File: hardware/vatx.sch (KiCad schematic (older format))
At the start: 26 parts, among them J1 USB, P1 CONN_10X2, P2 CONN_01X05, P3 CONN_1, P4 CONN_1, P5 CONN_1, P6 CONN_1, P7 CONN_1, SW1 SWITCH_INV, U1 LM317T

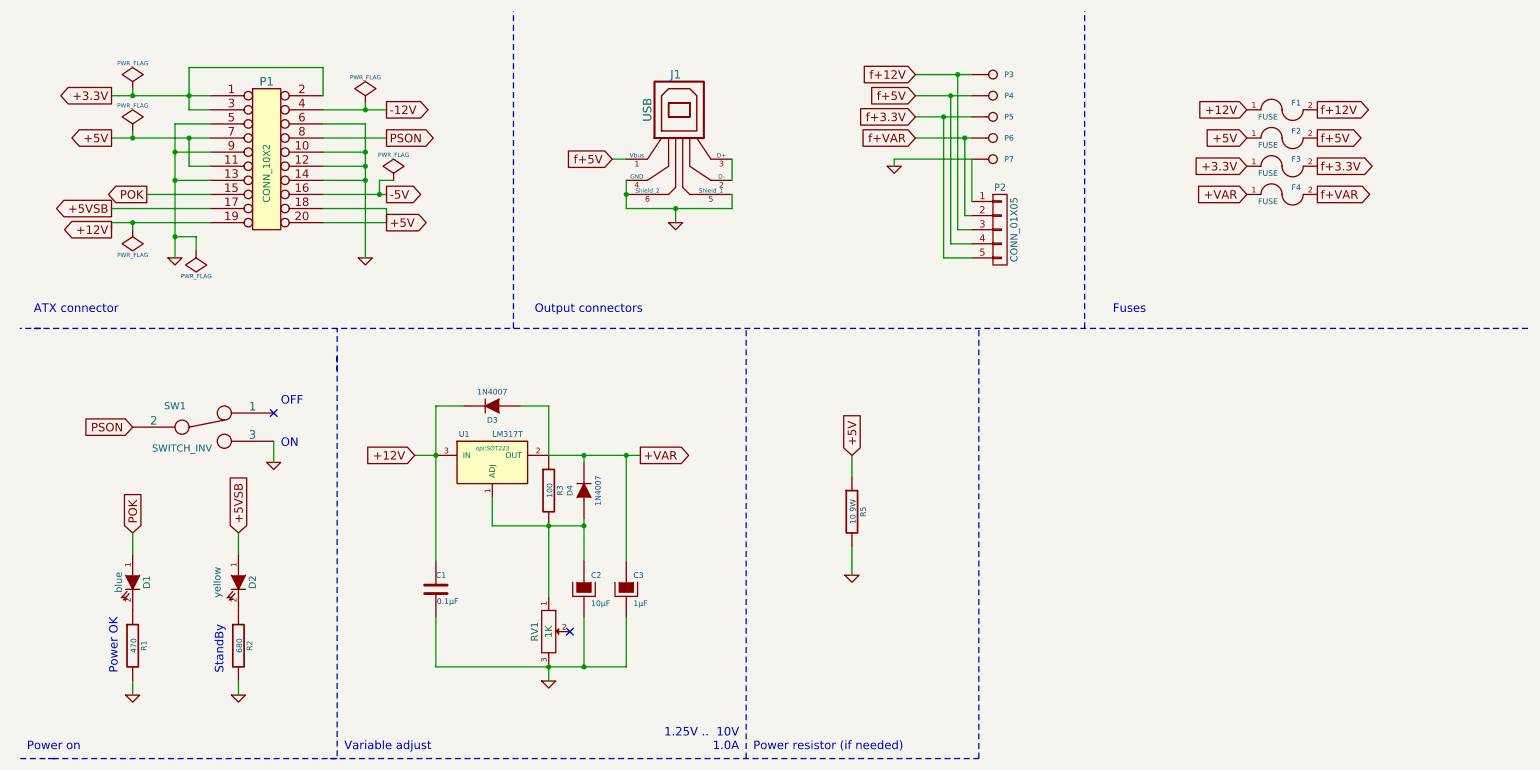
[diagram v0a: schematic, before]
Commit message: scheme for optional PSON control
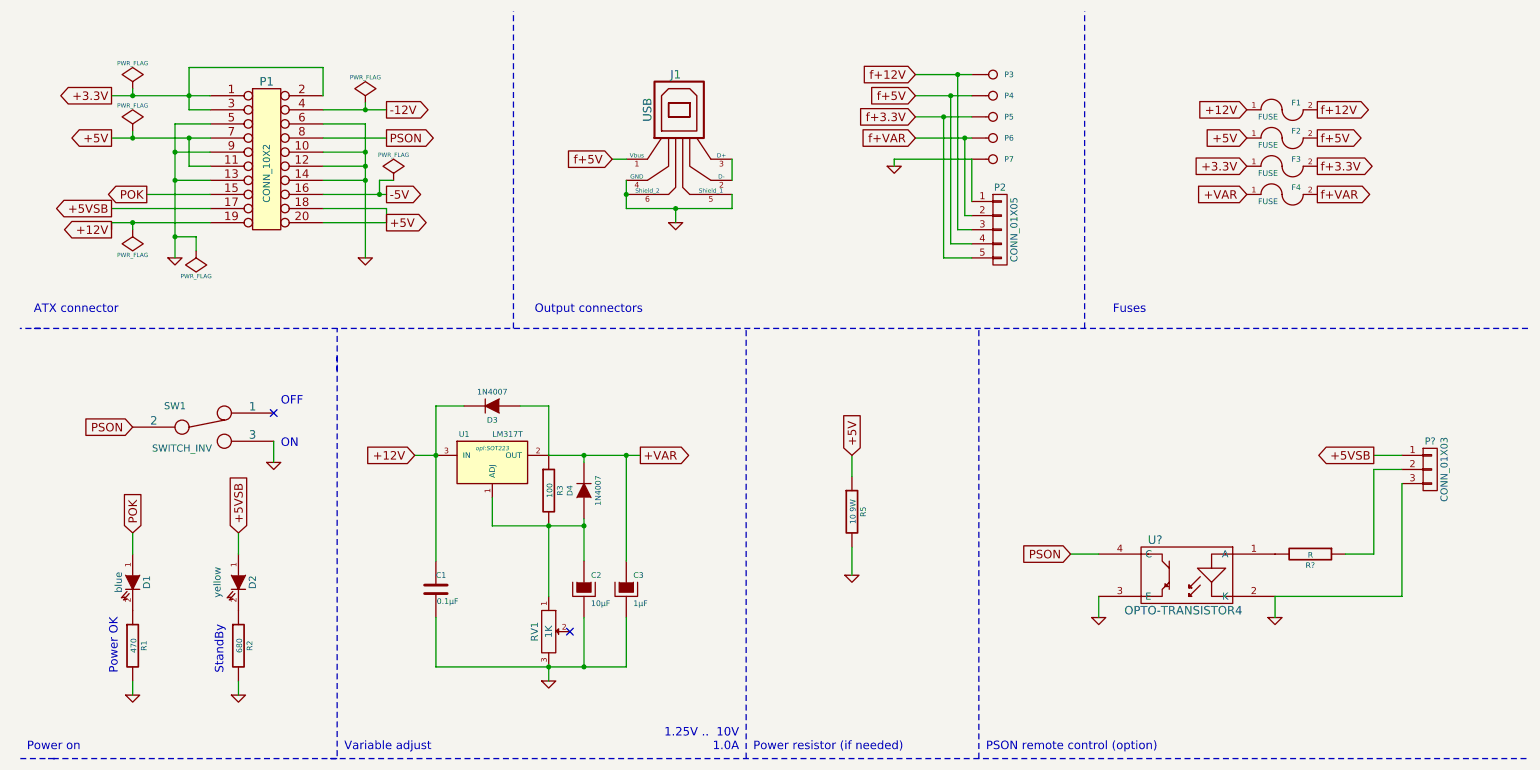
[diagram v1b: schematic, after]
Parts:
- added P?: CONN_01X03, symbol CONN_01X03
- added R?: R, symbol R
- added U?: OPTO-TRANSISTOR4, symbol OPTO-TRANSISTOR4
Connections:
- net +5VSB: now also P?.1 (P1)
- net GND: now also P?.3 (P3), U?.2 (K), U?.3 (E)
- net PSON: now also U?.4 (C)
- new net: R?.2, U?.1 (A)
- new net: P?.2 (P2), R?.1
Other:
- note added: "PSON remote control (option)"
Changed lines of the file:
@@
 Power on
 Wire Notes Line
-	2700 5800 7300 5800
+	2700 5800 11200 5800
 Wire Notes Line
 	5650 5800 5650 2750
@@
 	7050 2250 7050 1250
 Connection ~ 7050 1250
+$Comp
+L OPTO-TRANSISTOR4 U?
+U 1 1 55119CA8
+P 8750 4500
+F 0 "U?" H 8950 4750 60  0000 C CNN
+F 1 "OPTO-TRANSISTOR4" H 8750 4250 60  0000 C CNN
+F 2 "" H 8750 4500 60  0000 C CNN
+F 3 "" H 8750 4500 60  0000 C CNN
+	1    8750 4500
+	-1   0    0    -1
+$EndComp
+$Comp
+L R R?
+U 1 1 55119D2F
+P 9650 4350
+F 0 "R?" V 9730 4350 40  0000 C CNN
+F 1 "R" V 9657 4351 40  0000 C CNN
+F 2 "" V 9580 4350 30  0000 C CNN
+F 3 "" H 9650 4350 30  0000 C CNN
+	1    9650 4350
+	0    1    1    0
+$EndComp
+$Comp
+L GND #PWR?
+U 1 1 5511A127
+P 9400 4800
+F 0 "#PWR?" H 9400 4800 30  0001 C CNN
+F 1 "GND" H 9400 4730 30  0001 C CNN
+F 2 "" H 9400 4800 60  0000 C CNN
+F 3 "" H 9400 4800 60  0000 C CNN
+	1    9400 4800
+	1    0    0    -1
+$EndComp
+Wire Wire Line
+	9400 4650 9400 4800
+Text GLabel 7950 4350 0    60   Input ~ 0
+PSON
+$Comp
+L GND #PWR?
+U 1 1 5511A292
+P 8150 4800
+F 0 "#PWR?" H 8150 4800 30  0001 C CNN
+F 1 "GND" H 8150 4730 30  0001 C CNN
+F 2 "" H 8150 4800 60  0000 C CNN
+F 3 "" H 8150 4800 60  0000 C CNN
+	1    8150 4800
+	1    0    0    -1
+$EndComp
+Wire Wire Line
+	7950 4350 8150 4350
+Wire Wire Line
+	8150 4650 8150 4800
+Text GLabel 10100 3650 0    60   Output ~ 0
++5VSB
+$Comp
+L CONN_01X03 P?
+U 1 1 5511A632
+P 10500 3750
+F 0 "P?" H 10500 3950 50  0000 C CNN
+F 1 "CONN_01X03" V 10600 3750 50  0000 C CNN
+F 2 "" H 10500 3750 60  0000 C CNN
+F 3 "" H 10500 3750 60  0000 C CNN
+	1    10500 3750
+	1    0    0    -1
+$EndComp
+Wire Wire Line
+	10300 3650 10100 3650
+Wire Wire Line
+	10300 3750 10100 3750
+Wire Wire Line
+	10100 3750 10100 4350
+Wire Wire Line
+	10100 4350 9900 4350
+Wire Wire Line
+	10300 3850 10300 4650
+Wire Wire Line
+	10300 4650 9400 4650
+Text Notes 7350 5750 0    60   ~ 0
+PSON remote control (option)
 $EndSCHEMATC

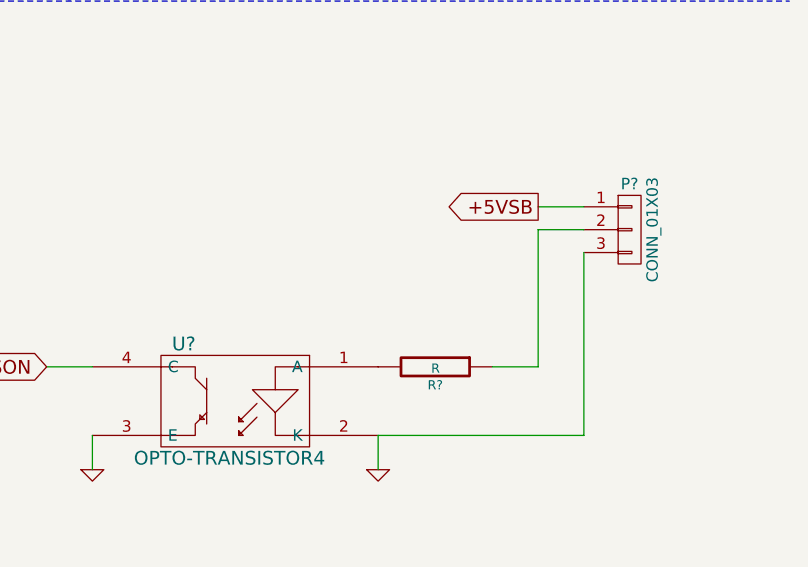
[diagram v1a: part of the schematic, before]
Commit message: pcb for optional PSON control
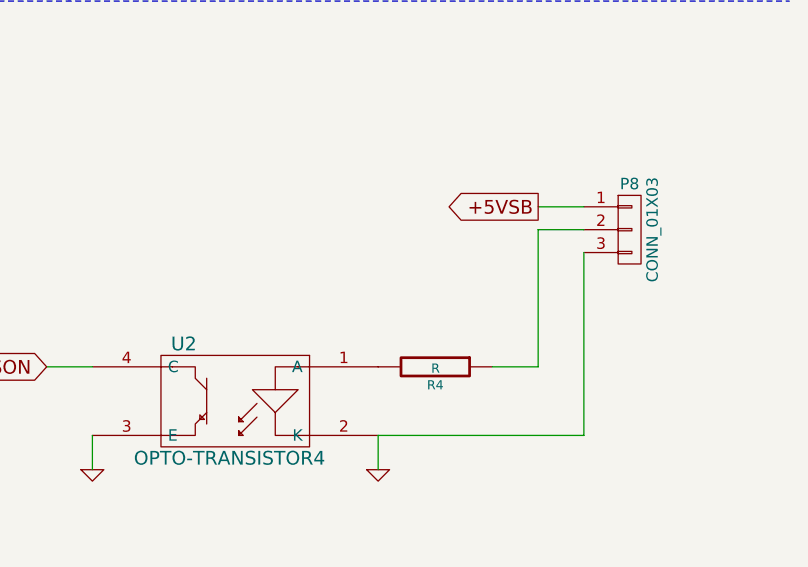
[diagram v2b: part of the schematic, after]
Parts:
- P8: renamed from P?; footprint (none) -> Pin_Headers:Pin_Header_Straight_1x03
- R4: renamed from R?; footprint (none) -> Resistors_SMD:R_0603_HandSoldering
- U2: renamed from U?; footprint (none) -> Opto-Devices:Optocoupler_SMD_HandSoldering_KPC357_LTV35x_PC357_SingleChannel
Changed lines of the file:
@@
 Sheet 1 1
 Title "VATX : Variable ATX Power Supply"
-Date "10 mars 2015"
-Rev "v2.0"
+Date "24 mars 2015"
+Rev "v2.1"
 Comp "Fablab Lannion"
 Comment1 "Jérôme Labidurie"
@@
 Connection ~ 7050 1250
 $Comp
-L OPTO-TRANSISTOR4 U?
+L OPTO-TRANSISTOR4 U2
 U 1 1 55119CA8
 P 8750 4500
-F 0 "U?" H 8950 4750 60  0000 C CNN
+F 0 "U2" H 8950 4750 60  0000 C CNN
 F 1 "OPTO-TRANSISTOR4" H 8750 4250 60  0000 C CNN
-F 2 "" H 8750 4500 60  0000 C CNN
+F 2 "Opto-Devices:Optocoupler_SMD_HandSoldering_KPC357_LTV35x_PC357_SingleChannel" H 8750 4500 60  0001 C CNN
 F 3 "" H 8750 4500 60  0000 C CNN
 	1    8750 4500
@@
 $EndComp
 $Comp
-L R R?
+L R R4
 U 1 1 55119D2F
 P 9650 4350
-F 0 "R?" V 9730 4350 40  0000 C CNN
+F 0 "R4" V 9730 4350 40  0000 C CNN
 F 1 "R" V 9657 4351 40  0000 C CNN
-F 2 "" V 9580 4350 30  0000 C CNN
+F 2 "Resistors_SMD:R_0603_HandSoldering" V 9580 4350 30  0001 C CNN
 F 3 "" H 9650 4350 30  0000 C CNN
 	1    9650 4350
@@
 $EndComp
 $Comp
-L GND #PWR?
+L GND #PWR016
 U 1 1 5511A127
 P 9400 4800
-F 0 "#PWR?" H 9400 4800 30  0001 C CNN
+F 0 "#PWR016" H 9400 4800 30  0001 C CNN
 F 1 "GND" H 9400 4730 30  0001 C CNN
 F 2 "" H 9400 4800 60  0000 C CNN
@@
 PSON
 $Comp
-L GND #PWR?
+L GND #PWR017
 U 1 1 5511A292
 P 8150 4800
-F 0 "#PWR?" H 8150 4800 30  0001 C CNN
+F 0 "#PWR017" H 8150 4800 30  0001 C CNN
 F 1 "GND" H 8150 4730 30  0001 C CNN
 F 2 "" H 8150 4800 60  0000 C CNN
@@
 +5VSB
 $Comp
-L CONN_01X03 P?
+L CONN_01X03 P8
 U 1 1 5511A632
 P 10500 3750
-F 0 "P?" H 10500 3950 50  0000 C CNN
+F 0 "P8" H 10500 3950 50  0000 C CNN
 F 1 "CONN_01X03" V 10600 3750 50  0000 C CNN
-F 2 "" H 10500 3750 60  0000 C CNN
+F 2 "Pin_Headers:Pin_Header_Straight_1x03" H 10500 3750 60  0001 C CNN
 F 3 "" H 10500 3750 60  0000 C CNN
 	1    10500 3750

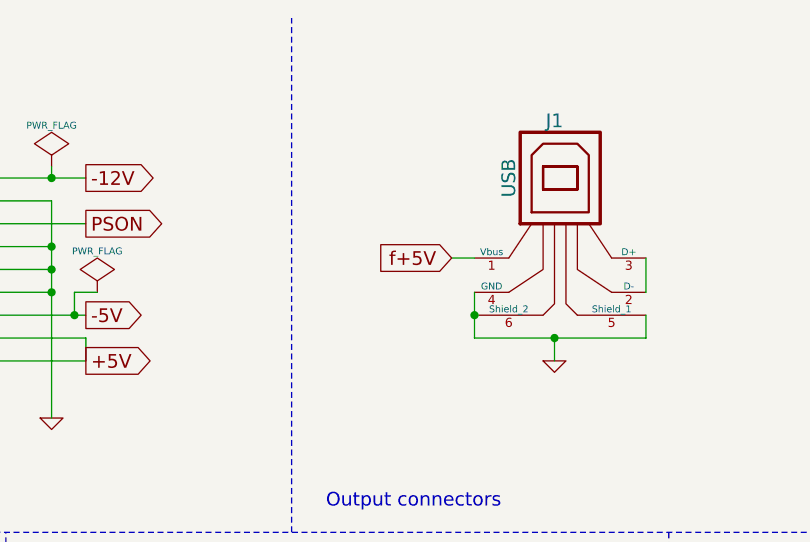
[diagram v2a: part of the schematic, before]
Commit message: Remove fuse for 5V usb
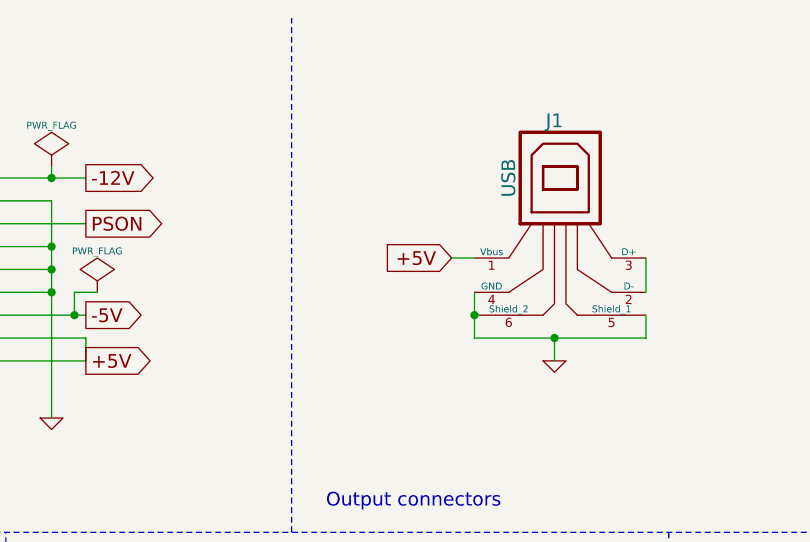
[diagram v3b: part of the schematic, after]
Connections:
- net +5V: now also J1.1 (Vbus)
- net f+5V: no longer J1.1 (Vbus)
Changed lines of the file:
@@
 Title "VATX : Variable ATX Power Supply"
 Date "24 mars 2015"
-Rev "v2.1"
+Rev "v2.2"
 Comp "Fablab Lannion"
 Comment1 "Jérôme Labidurie"
@@
 Wire Wire Line
 	6700 1550 6700 1600
-Text GLabel 4700 1550 0    60   Input ~ 0
-f+5V
 $Comp
 L GND #PWR08
@@
 Text Notes 7350 5750 0    60   ~ 0
 PSON remote control (option)
+Text GLabel 4700 1550 0    60   Input ~ 0
++5V
 $EndSCHEMATC

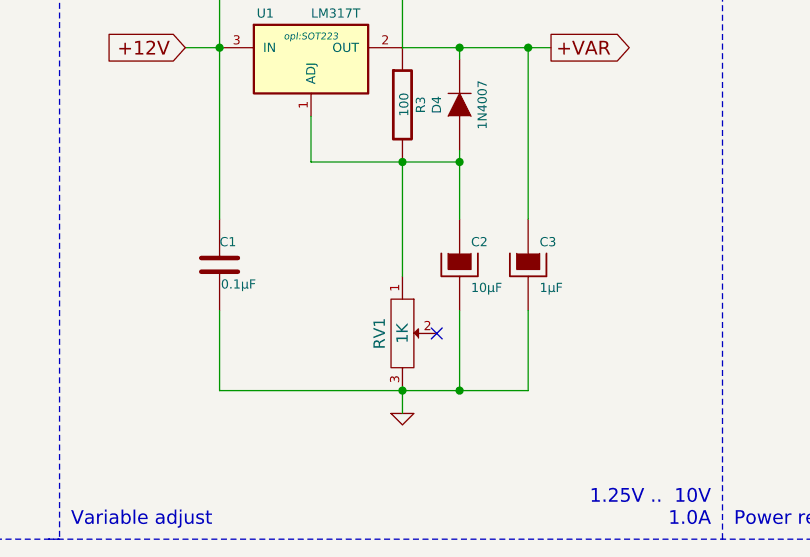
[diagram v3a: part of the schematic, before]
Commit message: V2.2 bugfix & enhancement * potentiometer connection * power/on silkscreen * more 0.8 traces for power traces (+12V, +5V) * more via for power traces (+5V, +3.3V)
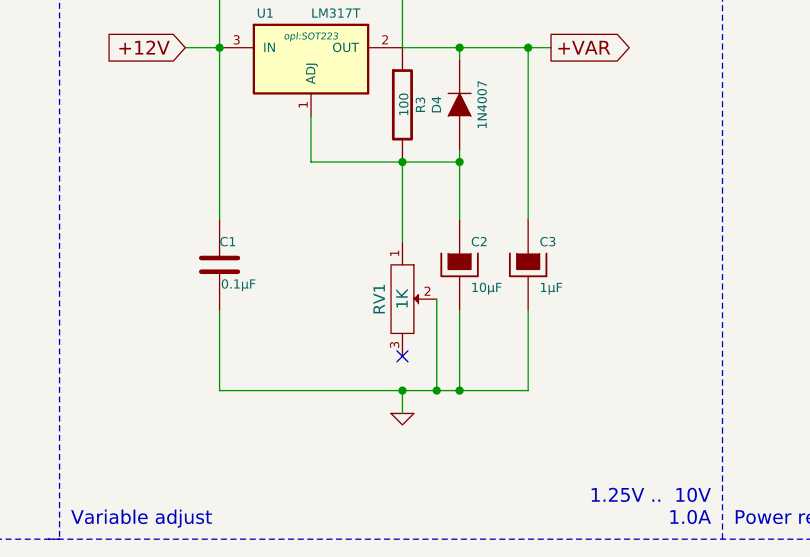
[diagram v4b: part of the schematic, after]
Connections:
- net GND: now also RV1.2; no longer RV1.3
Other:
- moved on the sheet: RV1
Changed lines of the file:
@@
 Sheet 1 1
 Title "VATX : Variable ATX Power Supply"
-Date "24 mars 2015"
-Rev "v2.2"
+Date "18 mai 2015"
+Rev "v2.3"
 Comp "Fablab Lannion"
 Comment1 "Jérôme Labidurie"
@@
 L POT RV1
 U 1 1 5345CFB7
-P 4250 4900
-F 0 "RV1" H 4250 4800 50  0000 C CNN
-F 1 "1K" H 4250 4900 50  0000 C CNN
-F 2 "Potentiometers:Potentiometer_Alps-RK16-single_largePads" H 4250 4900 60  0001 C CNN
-F 3 "" H 4250 4900 60  0000 C CNN
-	1    4250 4900
+P 4250 4750
+F 0 "RV1" H 4250 4650 50  0000 C CNN
+F 1 "1K" H 4250 4750 50  0000 C CNN
+F 2 "Potentiometers:Potentiometer_Alps-RK16-single_largePads" H 4250 4750 60  0001 C CNN
+F 3 "" H 4250 4750 60  0000 C CNN
+	1    4250 4750
 	0    1    1    0
 $EndComp
-Wire Wire Line
-	4250 5150 4250 5250
 Text GLabel 9200 1200 0    60   Input ~ 0
 +12V
@@
 Wire Wire Line
 	3450 4800 3450 5150
-Connection ~ 4250 5150
 $Comp
 L C C1
@@
 	1    0    0    -1
 $EndComp
-NoConn ~ 4400 4900
 $Comp
 L PWR_FLAG #FLG09
@@
 Text Notes 5700 5750 0    60   ~ 0
 Power resistor (if needed)
-Wire Wire Line
-	4250 4150 4250 4650
 $Comp
 L CONN_01X05 P2
@@
 Text GLabel 4700 1550 0    60   Input ~ 0
 +5V
+Wire Wire Line
+	4250 4500 4250 4150
+Wire Wire Line
+	4400 4750 4400 5150
+Connection ~ 4400 5150
+NoConn ~ 4250 5000
+Wire Wire Line
+	4250 5250 4250 5150
+Connection ~ 4250 5150
 $EndSCHEMATC
